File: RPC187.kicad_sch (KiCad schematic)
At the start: 22 parts, among them J2 USB_C, U1 STM32F411CEUx, U4 USBLC6-2SC6, U5 XC6206

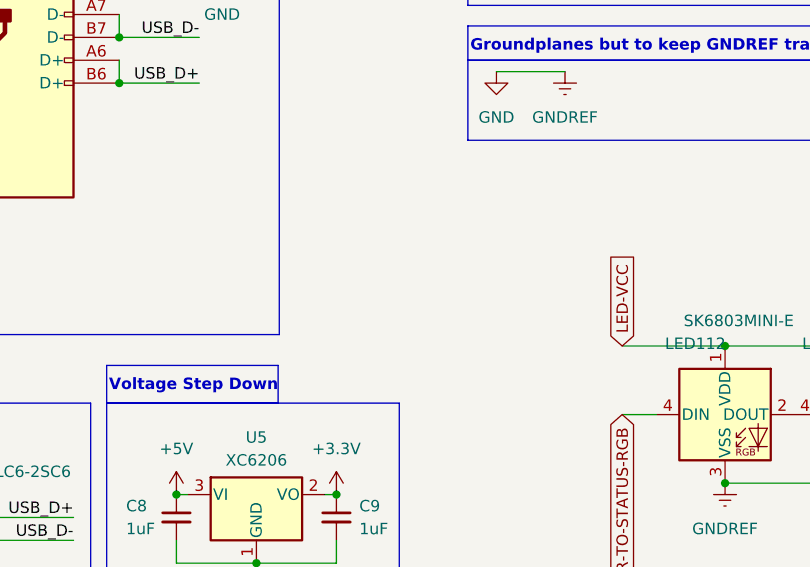
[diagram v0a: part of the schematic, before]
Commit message: All violations resolved, as much ground layer stitching done as I can. Revision 0.0.1, the rough cut.
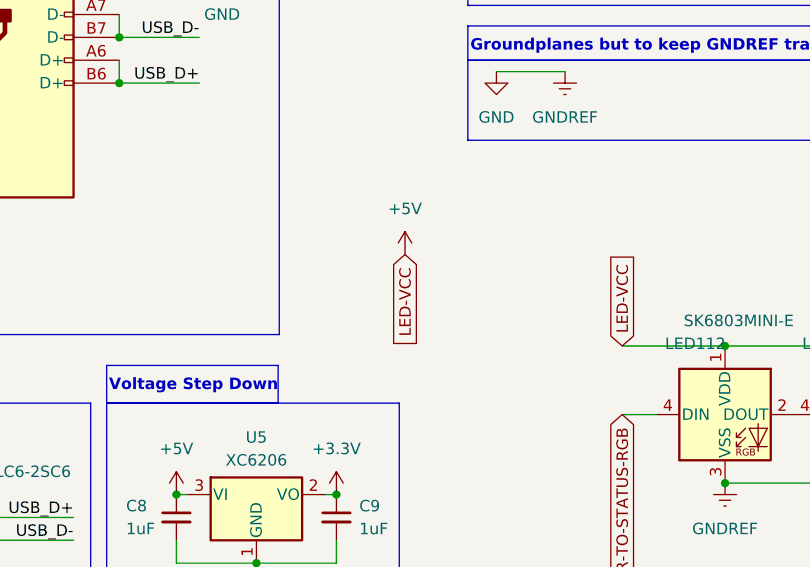
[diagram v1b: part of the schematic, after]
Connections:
- net LED-VCC is gone; now on net +5V: LED112.1 (VDD), LED113.1 (VDD)
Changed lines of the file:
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@@
+		)
+	)
+	(global_label "LED-VCC"
+		(shape input)
+		(at 229.87 87.63 270)
+		(fields_autoplaced yes)
+		(effects
+			(font
+				(size 1.27 1.27)
+			)
+			(justify right)
+		)
+		(property "Intersheetrefs" "${INTERSHEET_REFS}"
+			(at 229.87 99.2633 90)
+			(effects
+				(font
+					(size 1.27 1.27)
+				)
+				(justify right)
+				(hide yes)
+			)
 		)
 	)
@@
 			)
 		)
+	)
+	(symbol
+		(lib_id "power:+5V")
+		(at 229.87 87.63 0)
+		(unit 1)
+		(exclude_from_sim no)
+		(in_bom yes)
+		(on_board yes)
+		(dnp no)
+		(fields_autoplaced yes)
+		(property "Reference" "#PWR014"
+			(at 229.87 91.44 0)
+			(effects
+				(font
+					(size 1.27 1.27)
+				)
+				(hide yes)
+			)
+		)
+		(property "Value" "+5V"
+			(at 229.87 82.55 0)
+			(effects
+				(font
+					(size 1.27 1.27)
+				)
+			)
+		)
+		(property "Footprint" ""
+			(at 229.87 87.63 0)
+			(effects
+				(font
+					(size 1.27 1.27)
+				)
+				(hide yes)
+			)
+		)
+		(property "Datasheet" ""
+			(at 229.87 87.63 0)
+			(effects
+				(font
+					(size 1.27 1.27)
+				)
+				(hide yes)
+			)
+		)
+		(property "Description" "Power symbol creates a global label with name \"+5V\""
+			(at 229.87 87.63 0)
+			(effects
+				(font
+					(size 1.27 1.27)
+				)
+				(hide yes)
+			)
+		)
+		(pin "1"
+		)
+		(instances
+			(project "RPC187"
+				(path "/95a398a3-530a-498f-83e6-54659633b68d"
+					(reference "#PWR014")
+					(unit 1)
+				)
+			)
+		)

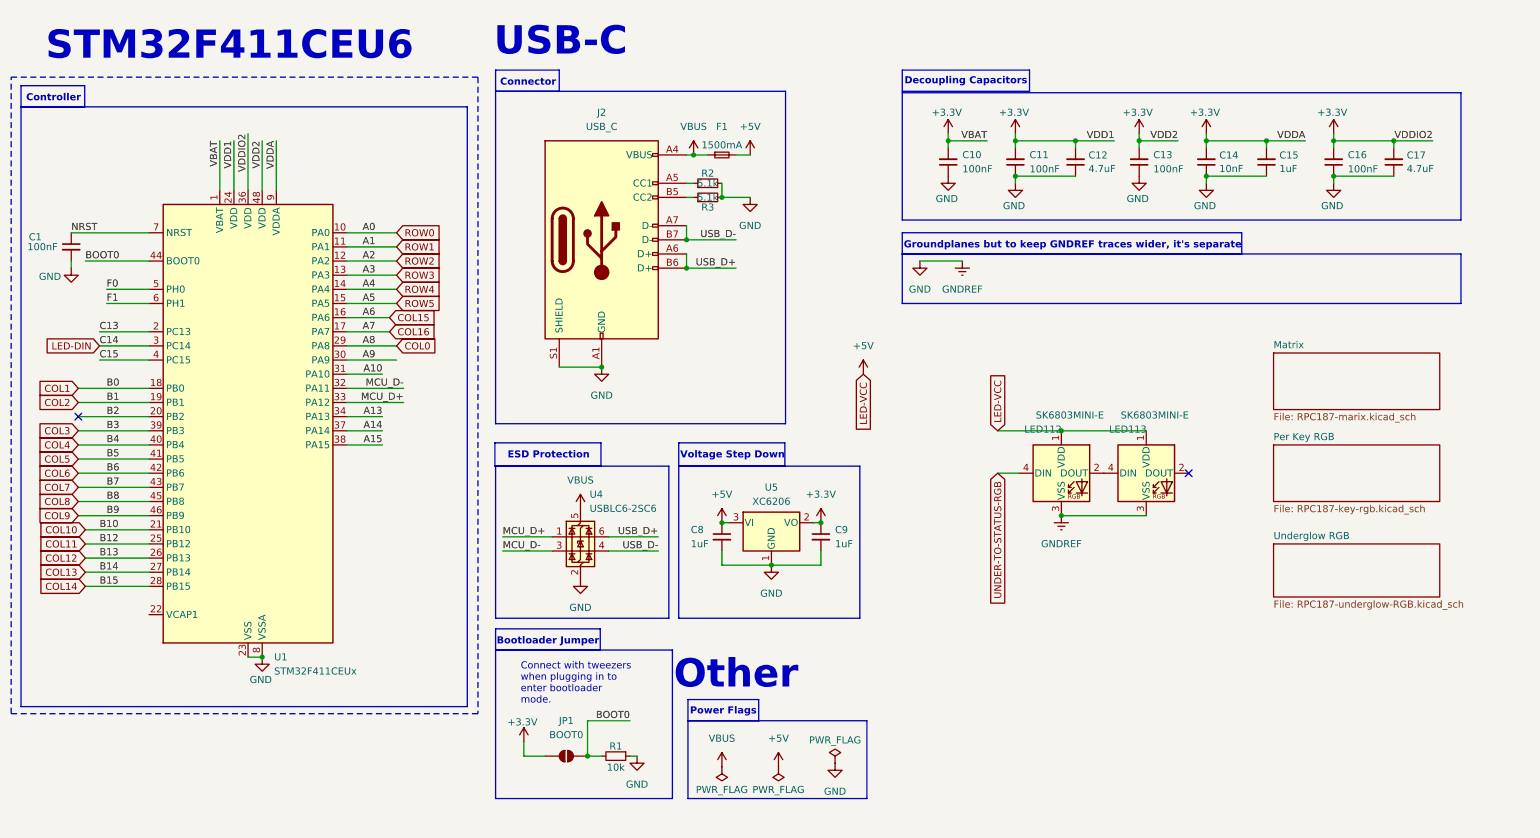
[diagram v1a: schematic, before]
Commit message: Wider LED VCC traces
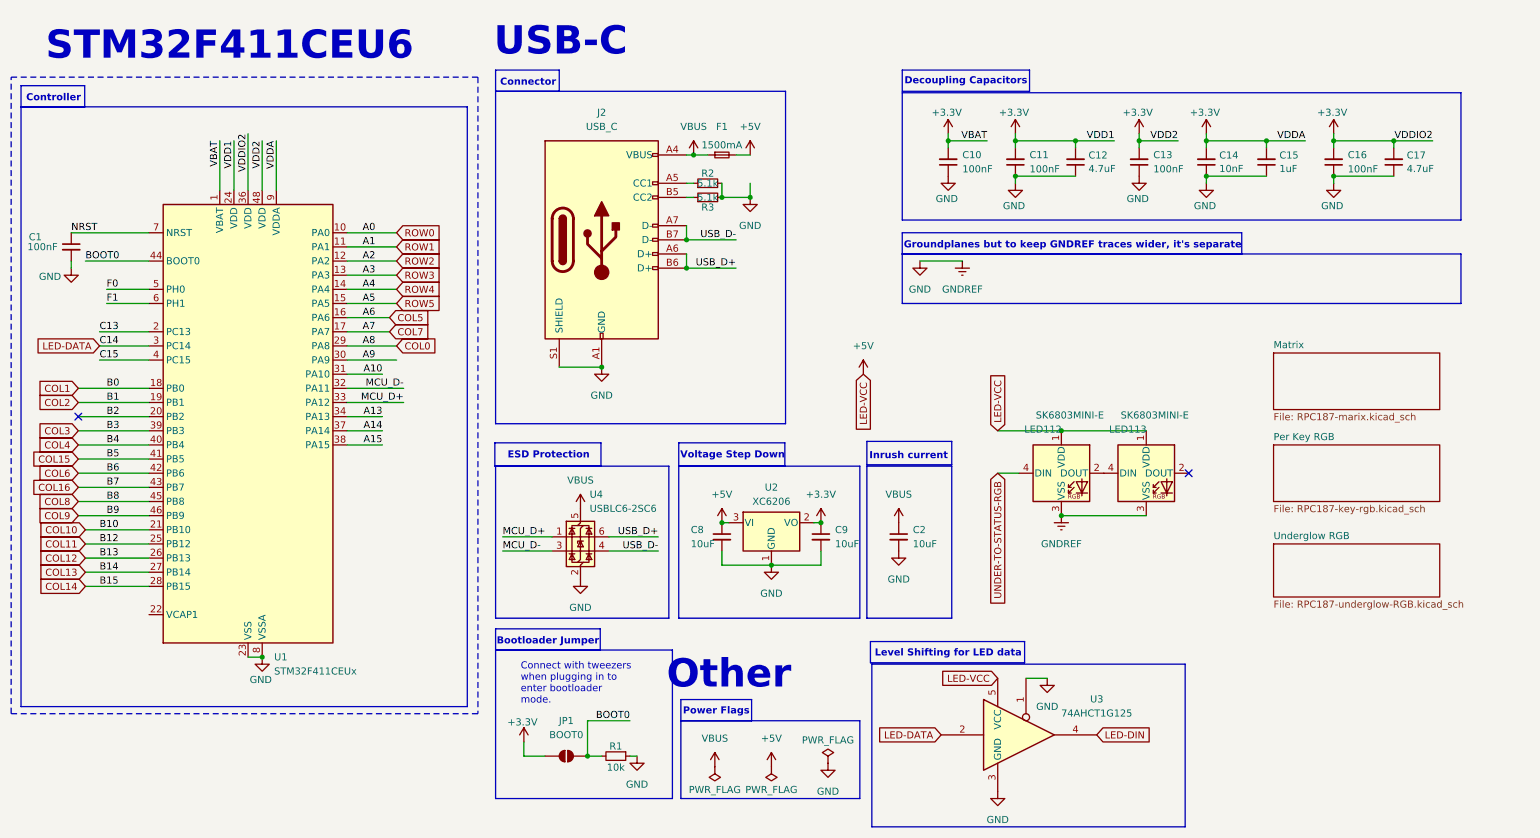
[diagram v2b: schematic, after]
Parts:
- added C2: 10uF, ScottoKeebs_Components:Capacitor_0402, symbol Device:C_Small
- added U3: 74AHCT1G125, Package_TO_SOT_SMD:SOT-23-5_HandSoldering, symbol 74xGxx:74AHCT1G125
- C8, C9: value 1uF -> 10uF
- renumbered U5 to U2
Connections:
- net +5V: now also U3.5 (VCC)
- net COL15: now also U1.41 (PB5); no longer U1.16 (PA6)
- net COL16: now also U1.43 (PB7); no longer U1.17 (PA7)
- net COL5: now also U1.16 (PA6); no longer U1.41 (PB5)
- net COL7: now also U1.17 (PA7); no longer U1.43 (PB7)
- net GND: now also C2.2, U3.1, U3.3 (GND)
- net LED-DIN: now also U3.4; no longer U1.3 (PC14)
- net VBUS: now also C2.1
- new net LED-DATA: U1.3 (PC14), U3.2
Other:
- note added: "Inrush current"
- note added: "Level Shifting for LED data"
